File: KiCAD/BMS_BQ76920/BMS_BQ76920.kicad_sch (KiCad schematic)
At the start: 5 parts, among them Q1 Q_NMOS, Q2 Q_NMOS, U2 STM32F103C8Tx

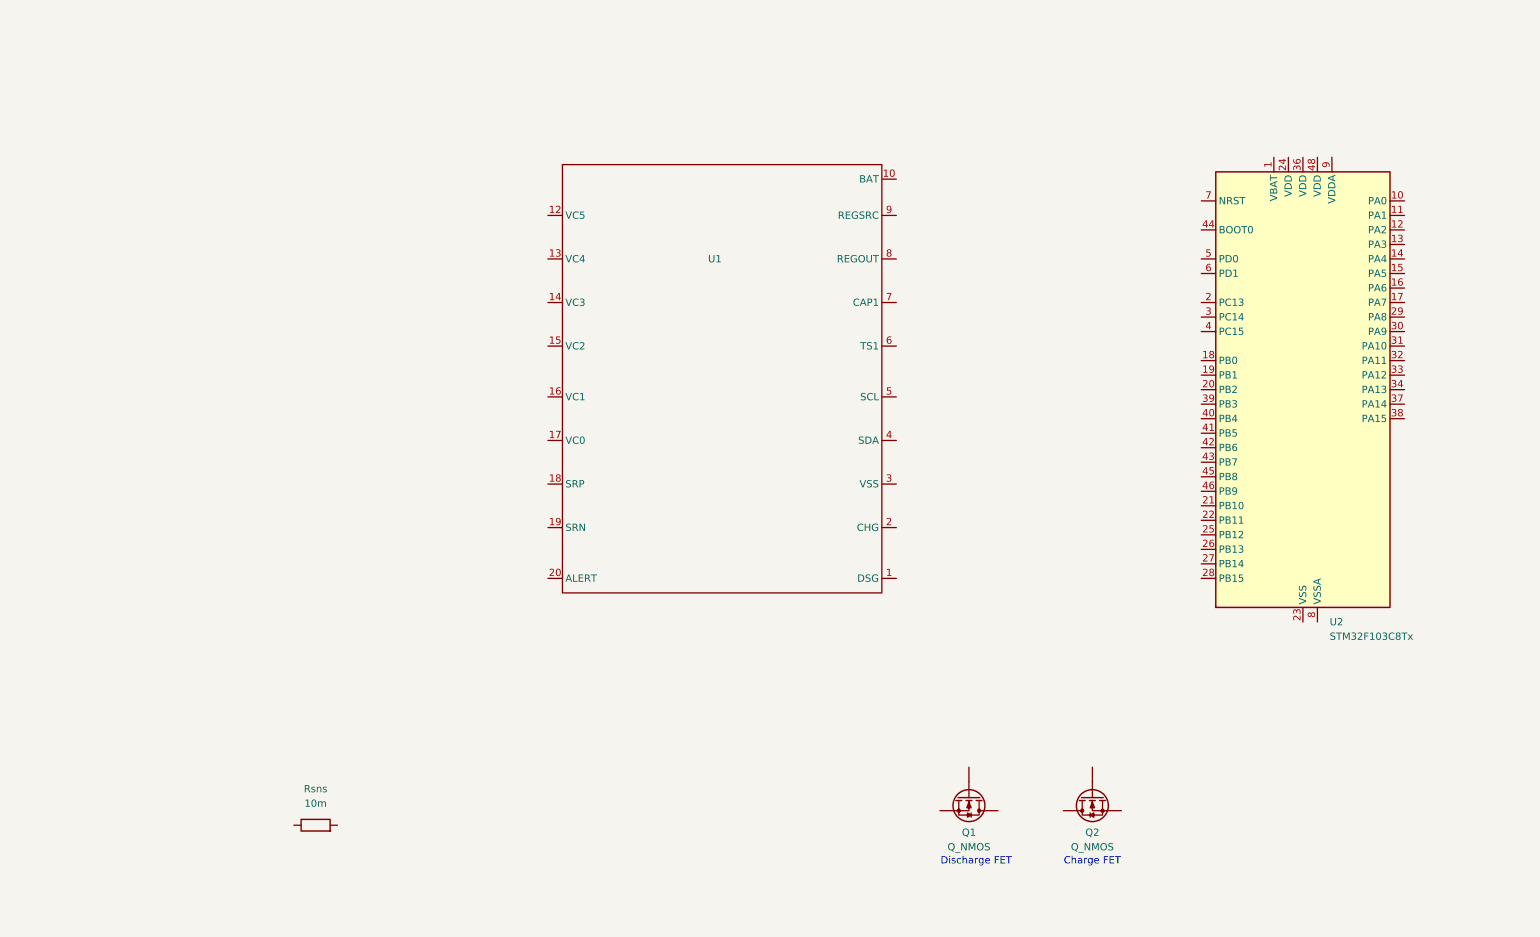
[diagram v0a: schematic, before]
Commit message: Place all schematic components - ready for wiring
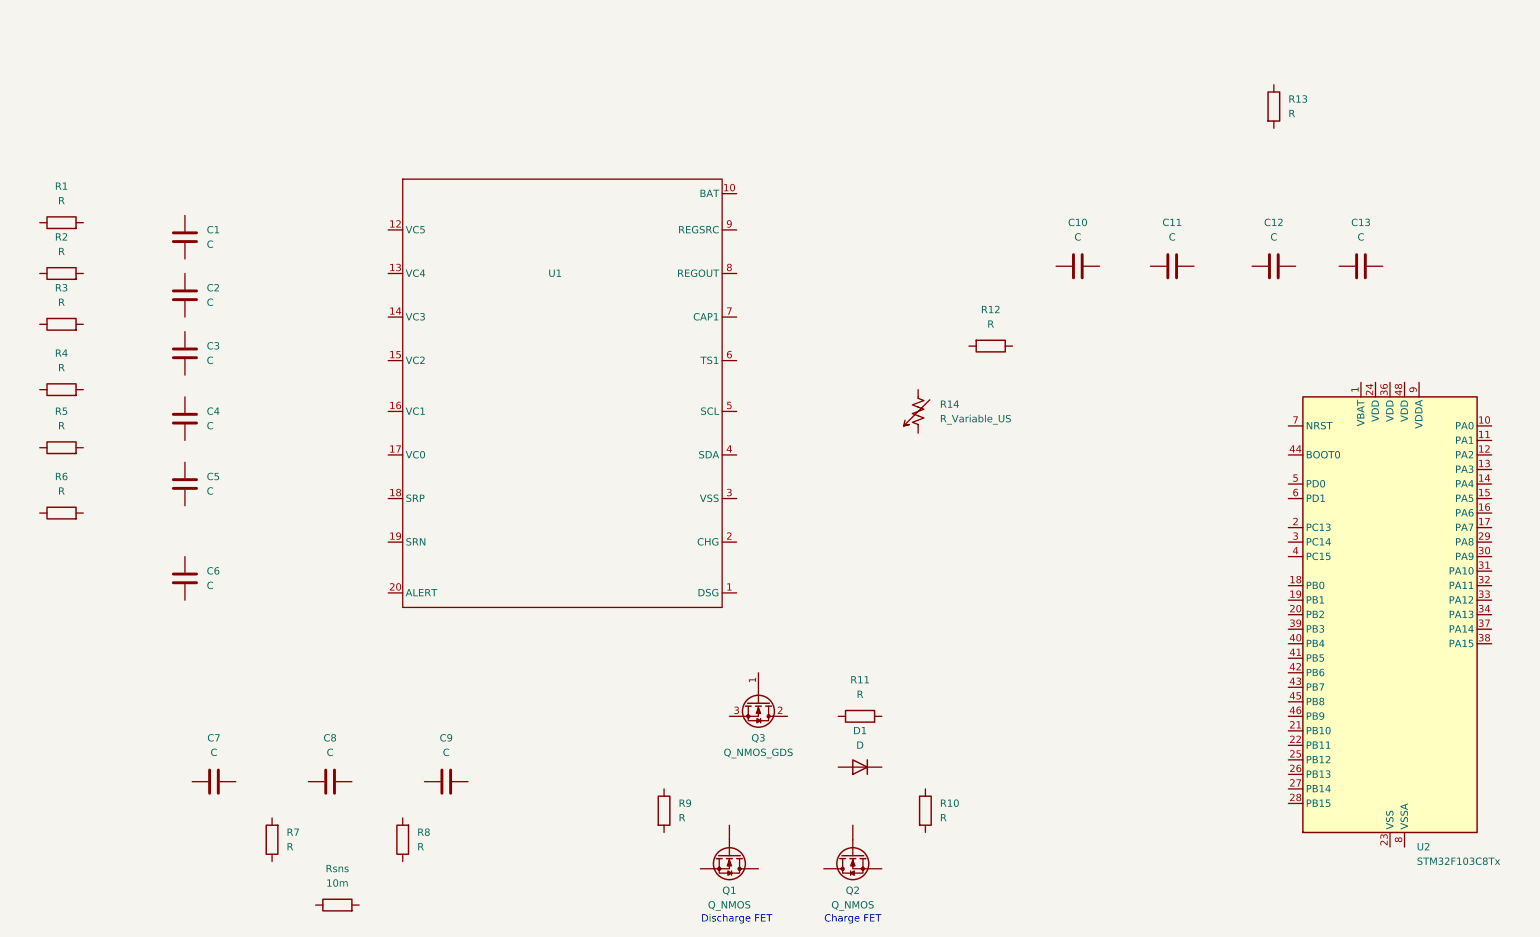
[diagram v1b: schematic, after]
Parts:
- added C1, C10, C11, C12, C13, C2, C3, C4, C5, C6, C7, C8, C9: C, symbol Device:C
- added D1: D, symbol Device:D
- added Q3: Q_NMOS_GDS, symbol Transistor_FET:Q_NMOS_GDS
- added R1, R10, R11, R12, R13, R2, R3, R4, R5, R6, R7, R8, R9: R, symbol Device:R
- added R14: R_Variable_US, symbol Device:R_Variable_US
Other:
- moved on the sheet: Q1, Q2, Rsns, U1, U2

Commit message: Schematic complete - ERC passed with zero errors
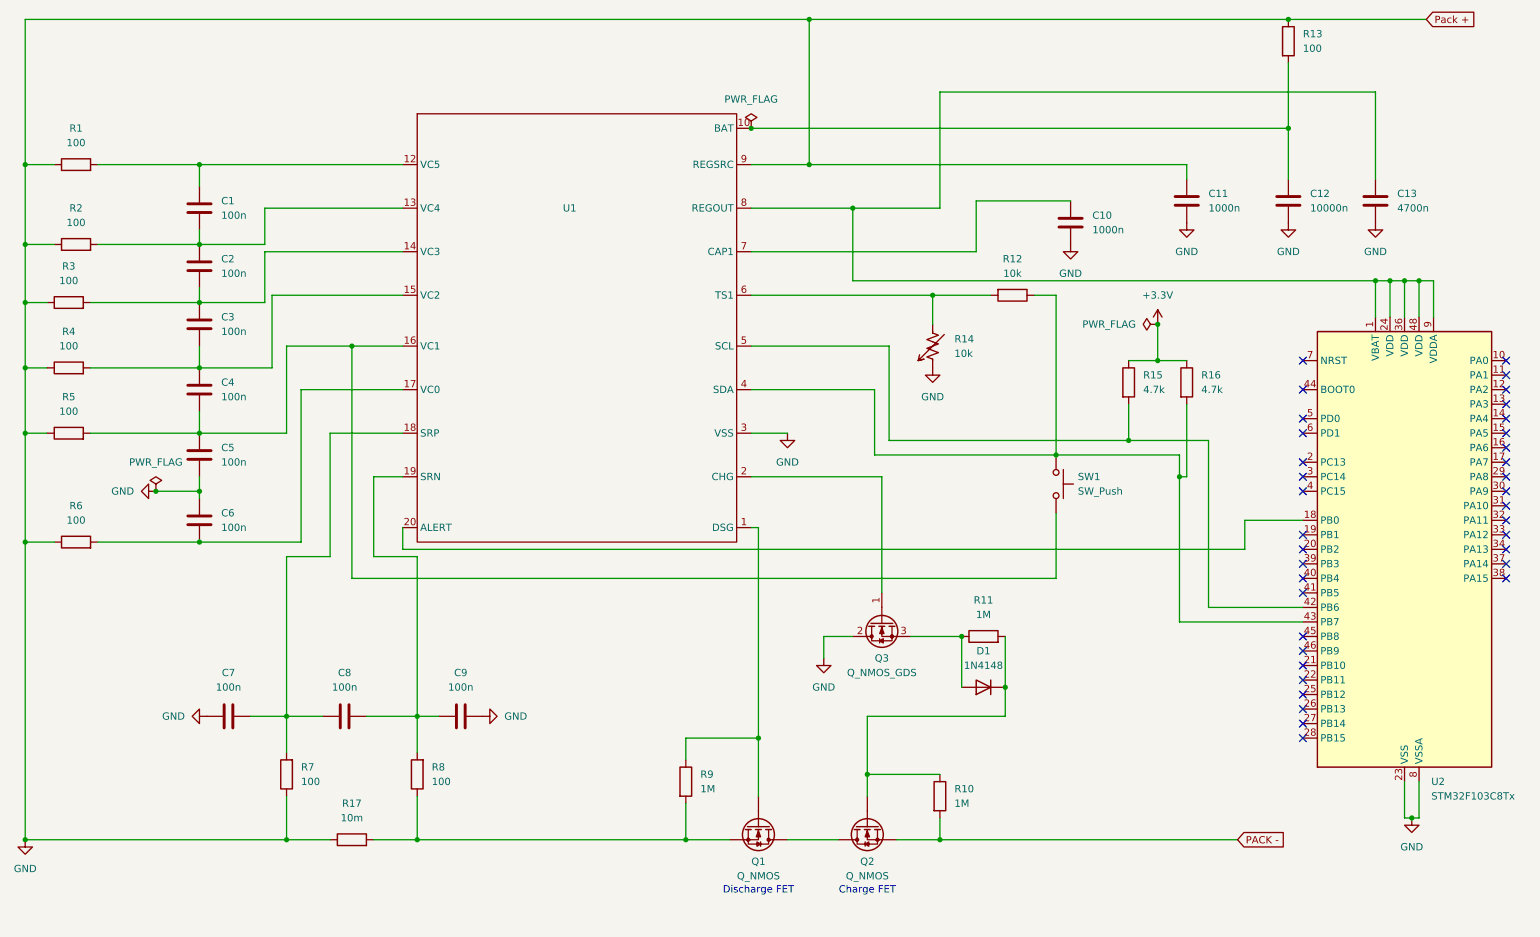
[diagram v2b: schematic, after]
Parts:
- added R15, R16: 4.7k, symbol Device:R
- added SW1: SW_Push, symbol Switch:SW_Push
- C1, C2, C3, C4, C5, C6, C7, C8, C9: value C -> 100n
- C10, C11: value C -> 1000n
- C12: value C -> 10000n
- C13: value C -> 4700n
- D1: value D -> 1N4148
- R1, R13, R2, R3, R4, R5, R6, R7, R8: value R -> 100
- R10, R11, R9: value R -> 1M
- R12: value R -> 10k
- R14: value R_Variable_US -> 10k
- renumbered Rsns to R17
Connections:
- net at R8.1: now also Q1.S, R17.2, R9.2
- net at R8.2: now also C8.2, C9.1, U1.19 (SRN)
- net GND: now reaches R2.1
- net GND: now also C10.1, C11.1, C11.2, C12.1, C13.1, C5.2, C6.1, C7.1, C9.2, Q3.2 (D), R1.1, R13.1, R14.1, R17.1, R3.1, R4.1, R5.1, R6.1, R7.1, U1.3 (VSS), U1.9 (REGSRC), U2.23 (VSS), U2.35 (VSS), U2.47 (VSS), U2.8 (VSSA)
- net at R2.2: now also C1.2, C2.1, U1.13 (VC4)
- net at C5.1: now also C4.2, R5.2, U1.16 (VC1), SW1.2
- net at D1.1 (K): now also Q2.G, R10.1, R11.2
- net at D1.2 (A): now also Q3.3 (S), R11.1
- net at R4.2: now also C3.2, C4.1, U1.15 (VC2)
- net at C8.1: now also C7.2, R7.2, U1.18 (SRP)
- net at C3.1: now also C2.2, R3.2, U1.14 (VC3)
- net at U1.1 (DSG): now also Q1.G, R9.1
- net at U1.10 (BAT): now also C12.2, R13.2
- net at U1.12 (VC5): now also C1.1, R1.2
- net at U1.17 (VC0): now also C6.2, R6.2
- net at U1.2 (CHG): now also Q3.1 (G)
- net at U1.20 (ALERT): now also U2.18 (PB0)
- net at U1.4 (SDA): now also R12.1, U2.43 (PB7), R16.2, SW1.1
- net at U1.5 (SCL): now also U2.42 (PB6), R15.2
- net at U1.6 (TS1): now also R12.2, R14.2
- net at U1.7 (CAP1): now also C10.2
- net at U1.8 (REGOUT): now also C13.2, U2.1 (VBAT), U2.24 (VDD), U2.36 (VDD), U2.48 (VDD), U2.9 (VDDA)
- net at Q2.D: now also Q1.D
- net PACK -: now reaches Q2.S
- net PACK -: now also R10.2
- new net +3.3V: R15.1, R16.1
- no-connect marks 0 -> 36
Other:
- moved on the sheet: C1, C10, C11, C12, C13, C2, C3, C4, C5, C6, C7, C8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

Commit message: All llaidout pcb editor
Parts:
- removed Q1, Q2: Q_NMOS, symbol Device:Q_NMOS
- added Q1, Q2: Q_NMOS_GDS, Package_TO_SOT_SMD:TSOT-23_HandSoldering, symbol Transistor_FET:Q_NMOS_GDS
- C1, C10, C11, C12, C13, C2, C3, C4, C5, C6, C7, C8, C9: footprint (none) -> Capacitor_SMD:C_0805_2012Metric
- D1: footprint (none) -> Diode_SMD:D_SOD-123
- Q3: footprint (none) -> Package_TO_SOT_SMD:TSOT-23_HandSoldering
- R1, R10, R11, R12, R13, R14, R15, R16, R17, R2, R3, R4, R5, R6, R7, R8, R9: footprint (none) -> Resistor_SMD:R_0805_2012Metric
- SW1: footprint (none) -> Button_Switch_THT:SW_PUSH_6mm_H4.3mm
- U1: footprint (none) -> Package_SO:TSSOP-20_4.4x6.5mm_P0.65mm
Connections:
- net PACK -: now also Q2.3 (S)
- net at R17.2, R8.1, R9.2: now also Q1.3 (S)
- net at D1.1 (K), R10.1, R11.2: now also Q2.1 (G)
- net at R9.1, U1.1 (DSG): now also Q1.1 (G)
- new net: Q1.2 (D), Q2.2 (D)
